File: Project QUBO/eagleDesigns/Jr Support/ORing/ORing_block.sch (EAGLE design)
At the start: 63 parts

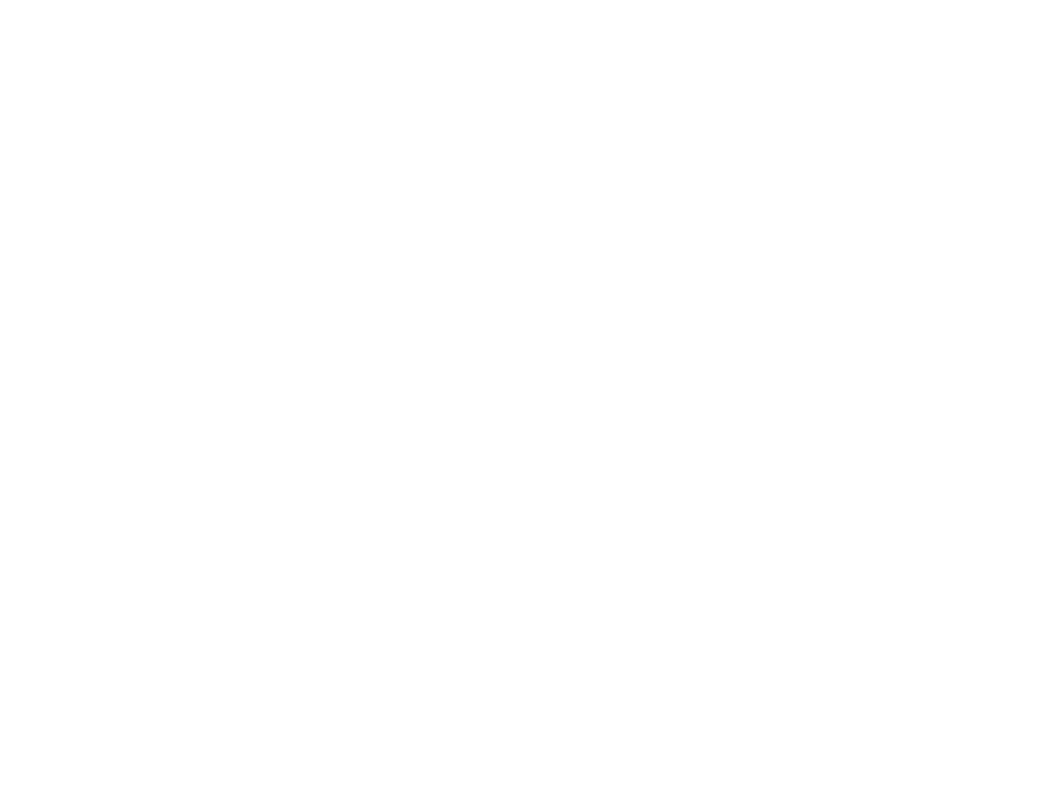
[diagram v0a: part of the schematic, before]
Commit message: 
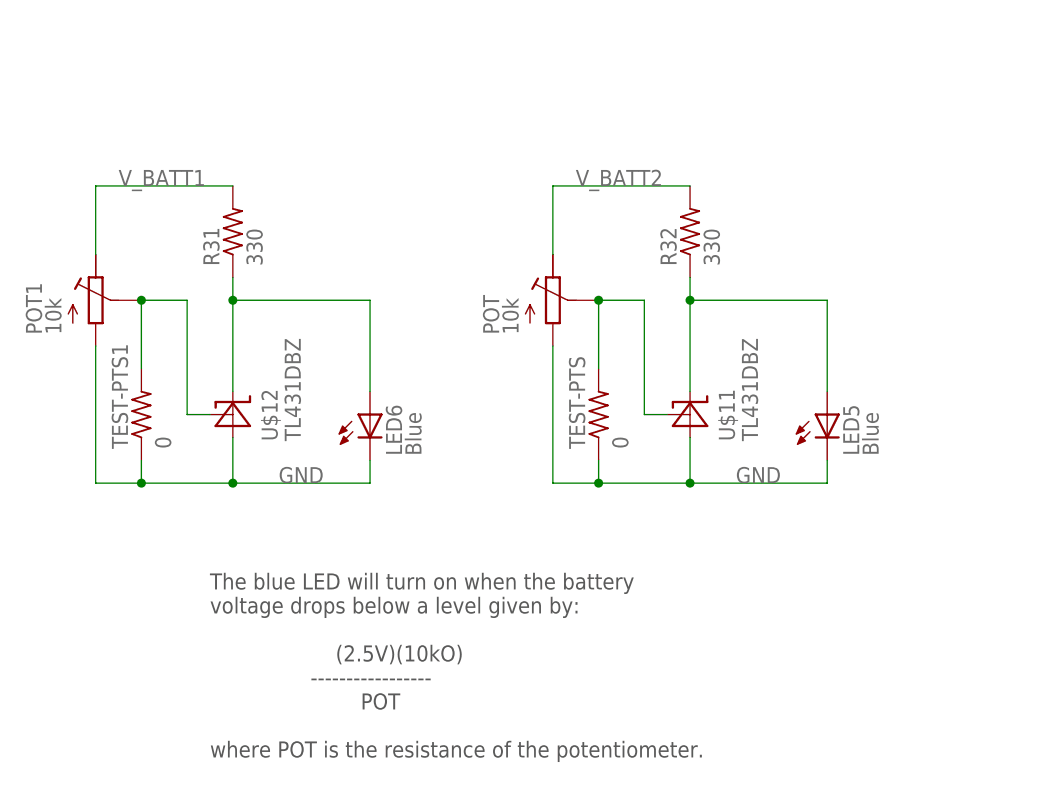
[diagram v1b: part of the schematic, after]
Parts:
- added LED5, LED6: Blue, led:0805_LED
- added POT, POT1: 10k, resistor:R-TRIMMPTV09A-4
- added R31, R32: 330, resistor:R-US_R0805
- added TEST-PTS, TEST-PTS1: 0, resistor:R-US_V526-0
- added U$11, U$12: TL431DBZ, texas:TL431DBZ
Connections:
- new net N$23: POT.S, TEST-PTS.2, U$11.REF
- new net N$30: LED5.A, R32.1, U$11.C
- new net N$31: POT1.S, TEST-PTS1.2, U$12.REF
- new net N$32: LED6.A, R31.1, U$12.C
- net GND: now also LED5.C, LED6.C, POT.E, POT1.E, TEST-PTS.1, TEST-PTS1.1, U$11.A, U$12.A
- net V_BATT1: now also POT1.A, R31.2
- net V_BATT2: now also POT.A, R32.2
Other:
- note added: "The blue LED will turn on when the battery voltage drops below a level given by: (2.5V)(10kO) ----------------- POT where POT is the resistance of the potentiometer."
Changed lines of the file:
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@@
 <part name="R30" library="resistor" deviceset="R-US_" device="R0805" value="20k+"/>
 <part name="LED4" library="led" deviceset="LED" device="CHIPLED_0805"/>
+<part name="U$11" library="texas" deviceset="TL431" device="DBZ"/>
+<part name="LED5" library="led" deviceset="0805_LED" device="" value="Blue"/>
+<part name="R32" library="resistor" deviceset="R-US_" device="R0805" value="330"/>
+<part name="POT" library="resistor" deviceset="R-TRIMM" device="PTV09A-4" value="10k"/>
+<part name="TEST-PTS" library="resistor" deviceset="R-US_" device="V526-0" value="0"/>
+<part name="U$12" library="texas" deviceset="TL431" device="DBZ"/>
+<part name="LED6" library="led" deviceset="0805_LED" device="" value="Blue"/>
+<part name="R31" library="resistor" deviceset="R-US_" device="R0805" value="330"/>
+<part name="POT1" library="resistor" deviceset="R-TRIMM" device="PTV09A-4" value="10k"/>
+<part name="TEST-PTS1" library="resistor" deviceset="R-US_" device="V526-0" value="0"/>
 </parts>
 <sheets>
 <sheet>
 <plain>
+<text x="-167.64" y="-190.5" size="1.778" layer="97">The blue LED will turn on when the battery
+voltage drops below a level given by:
+                    (2.5V)(10kO)
+                -----------------
+                        POT
+where POT is the resistance of the potentiometer.</text>
 </plain>
 <instances>
@@
 <instance part="R30" gate="G$1" x="66.04" y="-99.06" rot="R90"/>
 <instance part="LED4" gate="G$1" x="86.36" y="-78.74"/>
+<instance part="U$11" gate="G$1" x="-114.3" y="-152.4" rot="R90"/>
+<instance part="LED5" gate="G$1" x="-99.06" y="-152.4"/>
+<instance part="R32" gate="G$1" x="-114.3" y="-132.08" rot="R90"/>
+<instance part="POT" gate="G$1" x="-129.54" y="-139.7"/>
+<instance part="TEST-PTS" gate="G$1" x="-124.46" y="-152.4" rot="R90"/>
+<instance part="U$12" gate="G$1" x="-165.1" y="-152.4" rot="R90"/>
+<instance part="LED6" gate="G$1" x="-149.86" y="-152.4"/>
+<instance part="R31" gate="G$1" x="-165.1" y="-132.08" rot="R90"/>
+<instance part="POT1" gate="G$1" x="-180.34" y="-139.7"/>
+<instance part="TEST-PTS1" gate="G$1" x="-175.26" y="-152.4" rot="R90"/>
 </instances>
 <busses>
@@
 <wire x1="86.36" y1="-114.3" x2="78.74" y2="-114.3" width="0.1524" layer="91"/>
 <label x="81.28" y="-114.3" size="1.778" layer="95"/>
+</segment>
+<segment>
+<pinref part="TEST-PTS" gate="G$1" pin="1"/>
+<wire x1="-124.46" y1="-160.02" x2="-124.46" y2="-157.48" width="0.1524" layer="91"/>
+<pinref part="LED5" gate="G$1" pin="C"/>
+<wire x1="-124.46" y1="-160.02" x2="-114.3" y2="-160.02" width="0.1524" layer="91"/>
+<wire x1="-114.3" y1="-160.02" x2="-99.06" y2="-160.02" width="0.1524" layer="91"/>
+<wire x1="-99.06" y1="-160.02" x2="-99.06" y2="-157.48" width="0.1524" layer="91"/>
+<pinref part="POT" gate="G$1" pin="E"/>
+<wire x1="-129.54" y1="-144.78" x2="-129.54" y2="-160.02" width="0.1524" layer="91"/>
+<wire x1="-129.54" y1="-160.02" x2="-124.46" y2="-160.02" width="0.1524" layer="91"/>
+<junction x="-124.46" y="-160.02"/>
+<label x="-109.22" y="-160.02" size="1.778" layer="95"/>
+<pinref part="U$11" gate="G$1" pin="A"/>
+<wire x1="-114.3" y1="-154.94" x2="-114.3" y2="-160.02" width="0.1524" layer="91"/>
+<junction x="-114.3" y="-160.02"/>
+</segment>
+<segment>
+<pinref part="TEST-PTS1" gate="G$1" pin="1"/>
+<wire x1="-175.26" y1="-160.02" x2="-175.26" y2="-157.48" width="0.1524" layer="91"/>
+<pinref part="LED6" gate="G$1" pin="C"/>
+<wire x1="-175.26" y1="-160.02" x2="-165.1" y2="-160.02" width="0.1524" layer="91"/>
+<wire x1="-165.1" y1="-160.02" x2="-149.86" y2="-160.02" width="0.1524" layer="91"/>
+<wire x1="-149.86" y1="-160.02" x2="-149.86" y2="-157.48" width="0.1524" layer="91"/>
+<pinref part="POT1" gate="G$1" pin="E"/>
+<wire x1="-180.34" y1="-144.78" x2="-180.34" y2="-160.02" width="0.1524" layer="91"/>
+<wire x1="-180.34" y1="-160.02" x2="-175.26" y2="-160.02" width="0.1524" layer="91"/>
+<junction x="-175.26" y="-160.02"/>
+<label x="-160.02" y="-160.02" size="1.778" layer="95"/>
+<pinref part="U$12" gate="G$1" pin="A"/>
+<wire x1="-165.1" y1="-154.94" x2="-165.1" y2="-160.02" width="0.1524" layer="91"/>
+<junction x="-165.1" y="-160.02"/>
 </segment>
 </net>
@@
 <label x="96.52" y="25.4" size="1.778" layer="95"/>
 </segment>
+<segment>
+<pinref part="POT1" gate="G$1" pin="A"/>
+<pinref part="R31" gate="G$1" pin="2"/>
+<wire x1="-180.34" y1="-134.62" x2="-180.34" y2="-127" width="0.1524" layer="91"/>
+<wire x1="-180.34" y1="-127" x2="-165.1" y2="-127" width="0.1524" layer="91"/>
+<label x="-177.8" y="-127" size="1.778" layer="95"/>
+</segment>
 </net>
 <net name="V_BATT" class="0">
@@
 <label x="66.04" y="-91.44" size="1.778" layer="95"/>
 </segment>
+<segment>
+<pinref part="POT" gate="G$1" pin="A"/>
+<pinref part="R32" gate="G$1" pin="2"/>
+<wire x1="-129.54" y1="-134.62" x2="-129.54" y2="-127" width="0.1524" layer="91"/>
+<wire x1="-129.54" y1="-127" x2="-114.3" y2="-127" width="0.1524" layer="91"/>
+<label x="-127" y="-127" size="1.778" layer="95"/>
+</segment>
 </net>
 <net name="N$48" class="0">
@@
 </segment>
 </net>
+<net name="N$23" class="0">
+<segment>
+<pinref part="POT" gate="G$1" pin="S"/>
+<pinref part="TEST-PTS" gate="G$1" pin="2"/>
+<wire x1="-124.46" y1="-147.32" x2="-124.46" y2="-139.7" width="0.1524" layer="91"/>
+<pinref part="U$11" gate="G$1" pin="REF"/>
+<wire x1="-116.84" y1="-152.4" x2="-119.38" y2="-152.4" width="0.1524" layer="91"/>
+<wire x1="-119.38" y1="-152.4" x2="-119.38" y2="-139.7" width="0.1524" layer="91"/>
+<wire x1="-119.38" y1="-139.7" x2="-124.46" y2="-139.7" width="0.1524" layer="91"/>
+<junction x="-124.46" y="-139.7"/>
+</segment>
+</net>
+<net name="N$30" class="0">
+<segment>
+<pinref part="R32" gate="G$1" pin="1"/>
+<pinref part="U$11" gate="G$1" pin="C"/>
+<wire x1="-114.3" y1="-137.16" x2="-114.3" y2="-139.7" width="0.1524" layer="91"/>
+<pinref part="LED5" gate="G$1" pin="A"/>
+<wire x1="-114.3" y1="-139.7" x2="-114.3" y2="-149.86" width="0.1524" layer="91"/>
+<wire x1="-99.06" y1="-149.86" x2="-99.06" y2="-139.7" width="0.1524" layer="91"/>
+<wire x1="-114.3" y1="-139.7" x2="-99.06" y2="-139.7" width="0.1524" layer="91"/>
+<junction x="-114.3" y="-139.7"/>
+</segment>
+</net>
+<net name="N$31" class="0">
+<segment>
+<pinref part="POT1" gate="G$1" pin="S"/>
+<pinref part="TEST-PTS1" gate="G$1" pin="2"/>
+<wire x1="-175.26" y1="-147.32" x2="-175.26" y2="-139.7" width="0.1524" layer="91"/>
+<pinref part="U$12" gate="G$1" pin="REF"/>
+<wire x1="-167.64" y1="-152.4" x2="-170.18" y2="-152.4" width="0.1524" layer="91"/>
+<wire x1="-170.18" y1="-152.4" x2="-170.18" y2="-139.7" width="0.1524" layer="91"/>
+<wire x1="-170.18" y1="-139.7" x2="-175.26" y2="-139.7" width="0.1524" layer="91"/>
+<junction x="-175.26" y="-139.7"/>
+</segment>
+</net>
+<net name="N$32" class="0">
+<segment>
+<pinref part="R31" gate="G$1" pin="1"/>
+<pinref part="U$12" gate="G$1" pin="C"/>
+<wire x1="-165.1" y1="-137.16" x2="-165.1" y2="-139.7" width="0.1524" layer="91"/>
+<pinref part="LED6" gate="G$1" pin="A"/>
+<wire x1="-165.1" y1="-139.7" x2="-165.1" y2="-149.86" width="0.1524" layer="91"/>
+<wire x1="-149.86" y1="-149.86" x2="-149.86" y2="-139.7" width="0.1524" layer="91"/>
+<wire x1="-165.1" y1="-139.7" x2="-149.86" y2="-139.7" width="0.1524" layer="91"/>
+<junction x="-165.1" y="-139.7"/>
+</segment>
+</net>
 </nets>
 </sheet>
@@
 </schematic>
 </drawing>
+<compatibility>
+<note version="6.3" minversion="6.2.2" severity="warning">
+Since Version 6.2.2 text objects can contain more than one line,
+which will not be processed correctly with this version.
+</note>
+</compatibility>
 </eagle>

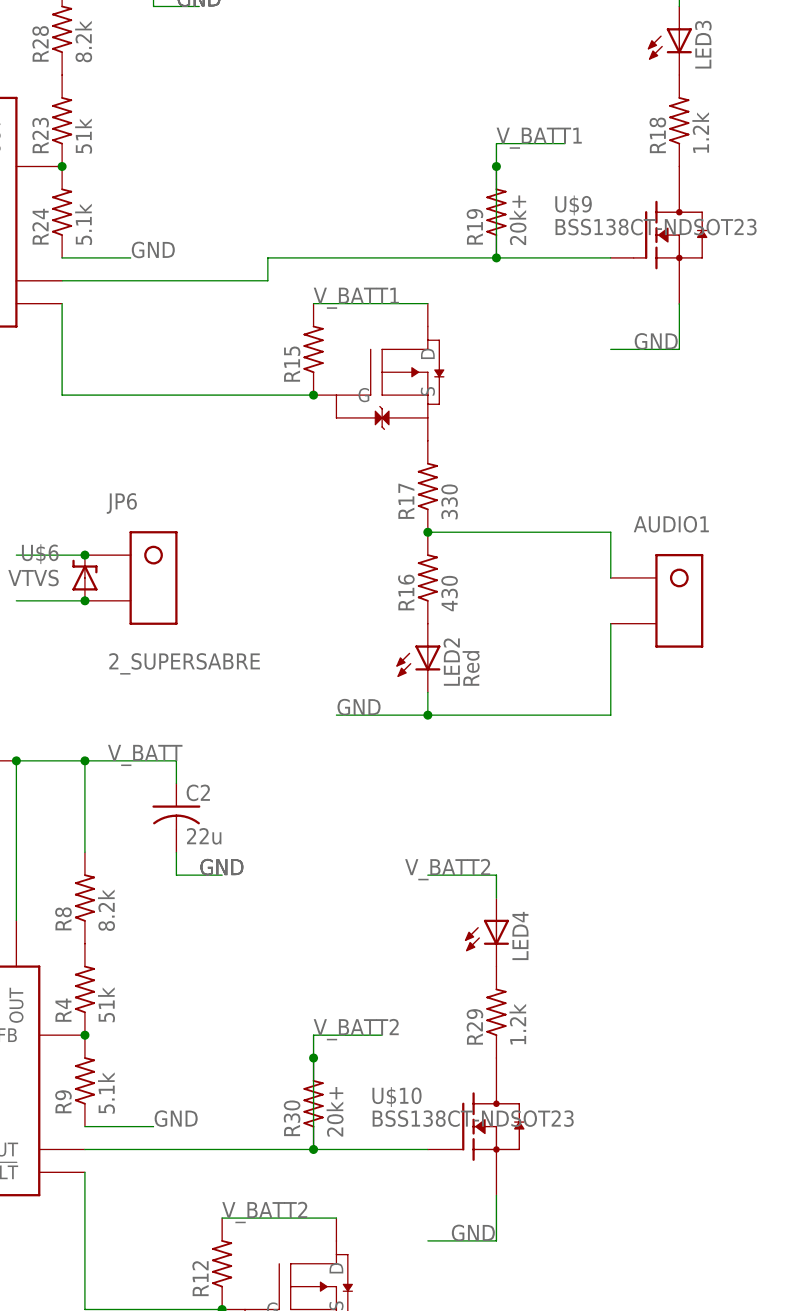
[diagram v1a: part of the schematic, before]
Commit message: 
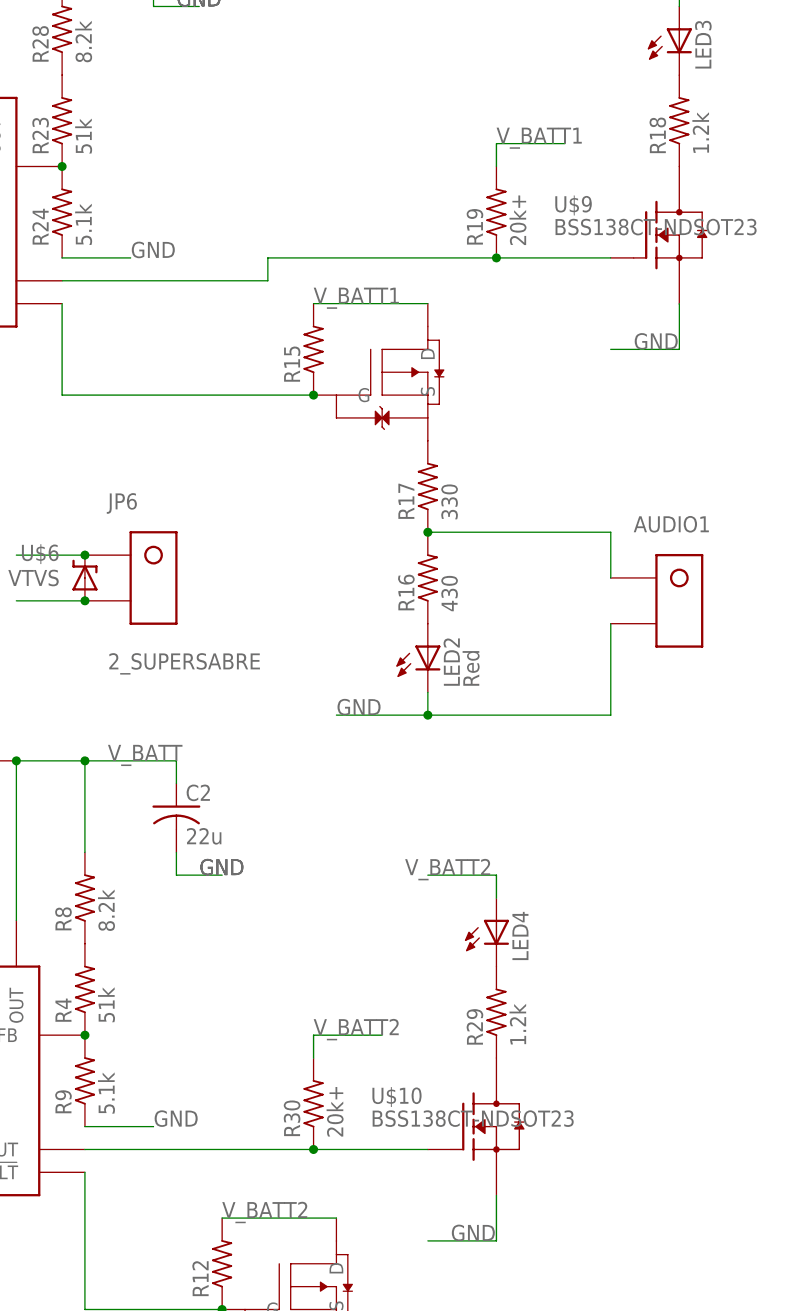
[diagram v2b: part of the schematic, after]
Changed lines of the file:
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@@
 <?xml version="1.0" encoding="utf-8"?>
 <!DOCTYPE eagle SYSTEM "eagle.dtd">
-<eagle version="8.1.0">
+<eagle version="8.0.0">
 <drawing>
 <settings>
@@
 <pinref part="R19" gate="G$1" pin="1"/>
 <wire x1="99.06" y1="-5.08" x2="86.36" y2="-5.08" width="0.1524" layer="91"/>
-<pinref part="R19" gate="G$1" pin="2"/>
-<wire x1="86.36" y1="-5.08" x2="86.36" y2="5.08" width="0.1524" layer="91"/>
 <junction x="86.36" y="-5.08"/>
-<wire x1="86.36" y1="5.08" x2="86.36" y2="7.62" width="0.1524" layer="91"/>
-<wire x1="86.36" y1="7.62" x2="93.98" y2="7.62" width="0.1524" layer="91"/>
-<junction x="86.36" y="5.08"/>
 <pinref part="U$27" gate="G$1" pin="ENOUT"/>
 <wire x1="38.1" y1="-7.62" x2="60.96" y2="-7.62" width="0.1524" layer="91"/>
 <wire x1="60.96" y1="-7.62" x2="60.96" y2="-5.08" width="0.1524" layer="91"/>
 <wire x1="60.96" y1="-5.08" x2="86.36" y2="-5.08" width="0.1524" layer="91"/>
-<label x="86.36" y="7.62" size="1.778" layer="95"/>
 </segment>
 <segment>
@@
 <wire x1="-180.34" y1="-127" x2="-165.1" y2="-127" width="0.1524" layer="91"/>
 <label x="-177.8" y="-127" size="1.778" layer="95"/>
+</segment>
+<segment>
+<wire x1="86.36" y1="7.62" x2="93.98" y2="7.62" width="0.1524" layer="91"/>
+<pinref part="R19" gate="G$1" pin="2"/>
+<wire x1="86.36" y1="5.08" x2="86.36" y2="7.62" width="0.1524" layer="91"/>
+<label x="86.36" y="7.62" size="1.778" layer="95"/>
 </segment>
 </net>
@@
 <pinref part="R30" gate="G$1" pin="1"/>
 <wire x1="78.74" y1="-104.14" x2="66.04" y2="-104.14" width="0.1524" layer="91"/>
-<pinref part="R30" gate="G$1" pin="2"/>
-<wire x1="66.04" y1="-104.14" x2="66.04" y2="-93.98" width="0.1524" layer="91"/>
 <junction x="66.04" y="-104.14"/>
-<wire x1="66.04" y1="-93.98" x2="66.04" y2="-91.44" width="0.1524" layer="91"/>
-<wire x1="66.04" y1="-91.44" x2="73.66" y2="-91.44" width="0.1524" layer="91"/>
-<junction x="66.04" y="-93.98"/>
 <wire x1="40.64" y1="-104.14" x2="66.04" y2="-104.14" width="0.1524" layer="91"/>
-<label x="66.04" y="-91.44" size="1.778" layer="95"/>
 </segment>
 <segment>
@@
 <label x="-127" y="-127" size="1.778" layer="95"/>
 </segment>
-</net>
+<segment>
+<pinref part="R30" gate="G$1" pin="2"/>
+<wire x1="66.04" y1="-93.98" x2="66.04" y2="-91.44" width="0.1524" layer="91"/>
+<wire x1="66.04" y1="-91.44" x2="73.66" y2="-91.44" width="0.1524" layer="91"/>
+<label x="66.04" y="-91.44" size="1.778" layer="95"/>
+</segment>
+</net>

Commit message: 
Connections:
- new net N$28: R30.1, U$1.ENOUT, U$10.G
- new net N$29: R19.1, U$27.ENOUT, U$9.G
- net V_BATT1: no longer R19.1, U$27.ENOUT, U$9.G
- net V_BATT2: no longer R30.1, U$10.G
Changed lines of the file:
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@@
-</segment>
-<segment>
-<pinref part="U$9" gate="G$1" pin="G"/>
-<pinref part="R19" gate="G$1" pin="1"/>
-<wire x1="99.06" y1="-5.08" x2="86.36" y2="-5.08" width="0.1524" layer="91"/>
-<junction x="86.36" y="-5.08"/>
-<pinref part="U$27" gate="G$1" pin="ENOUT"/>
-<wire x1="38.1" y1="-7.62" x2="60.96" y2="-7.62" width="0.1524" layer="91"/>
-<wire x1="60.96" y1="-7.62" x2="60.96" y2="-5.08" width="0.1524" layer="91"/>
-<wire x1="60.96" y1="-5.08" x2="86.36" y2="-5.08" width="0.1524" layer="91"/>
 </segment>
 <segment>
@@
 </segment>
 <segment>
-<pinref part="U$10" gate="G$1" pin="G"/>
-<pinref part="R30" gate="G$1" pin="1"/>
-<wire x1="78.74" y1="-104.14" x2="66.04" y2="-104.14" width="0.1524" layer="91"/>
-<junction x="66.04" y="-104.14"/>
-<wire x1="40.64" y1="-104.14" x2="66.04" y2="-104.14" width="0.1524" layer="91"/>
-</segment>
-<segment>
 <pinref part="POT" gate="G$1" pin="A"/>
 <pinref part="R32" gate="G$1" pin="2"/>
@@
 </segment>
 </net>
+<net name="N$28" class="0">
+<segment>
+<pinref part="U$1" gate="G$1" pin="ENOUT"/>
+<pinref part="U$10" gate="G$1" pin="G"/>
+<wire x1="40.64" y1="-104.14" x2="66.04" y2="-104.14" width="0.1524" layer="91"/>
+<pinref part="R30" gate="G$1" pin="1"/>
+<junction x="66.04" y="-104.14"/>
+<wire x1="66.04" y1="-104.14" x2="78.74" y2="-104.14" width="0.1524" layer="91"/>
+</segment>
+</net>
+<net name="N$29" class="0">
+<segment>
+<pinref part="U$27" gate="G$1" pin="ENOUT"/>
+<wire x1="38.1" y1="-7.62" x2="60.96" y2="-7.62" width="0.1524" layer="91"/>
+<wire x1="60.96" y1="-7.62" x2="60.96" y2="-5.08" width="0.1524" layer="91"/>
+<pinref part="R19" gate="G$1" pin="1"/>
+<wire x1="60.96" y1="-5.08" x2="86.36" y2="-5.08" width="0.1524" layer="91"/>
+<pinref part="U$9" gate="G$1" pin="G"/>
+<wire x1="86.36" y1="-5.08" x2="99.06" y2="-5.08" width="0.1524" layer="91"/>
+<junction x="86.36" y="-5.08"/>
+</segment>
+</net>
